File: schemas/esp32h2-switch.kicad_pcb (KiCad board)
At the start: 2 copper layers, 80.6 x 59.1 mm, 21 parts, among them J1 Screw_Terminal_01x02, J2 Screw_Terminal_01x02, J3 Conn_01x15, J4 Conn_01x15, K1 SPDT, 5V 72R, 10A 250VAC, Q1 NPN, 40V, 500mA, U1 LM1117MP-3.3

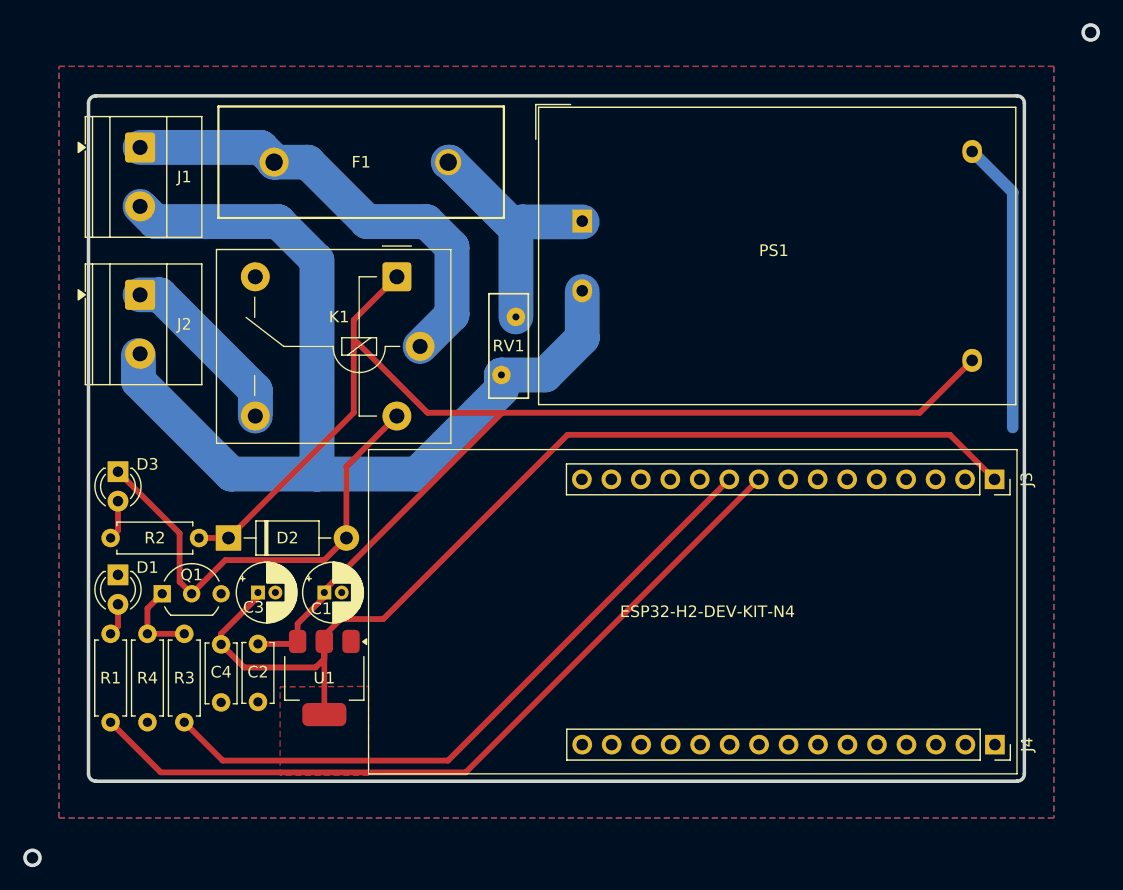
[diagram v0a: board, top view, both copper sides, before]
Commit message: Fix footprints and improve layout for hand soldering
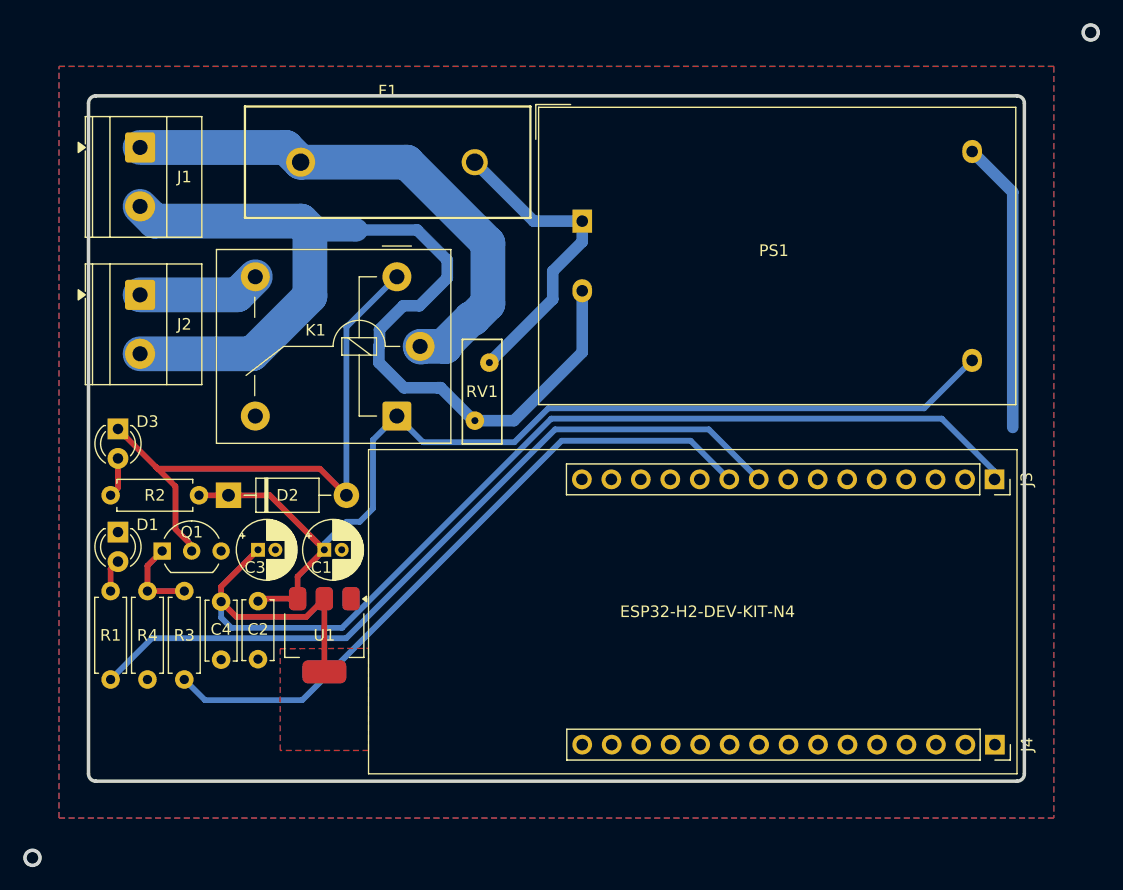
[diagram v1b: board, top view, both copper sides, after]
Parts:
- added NT1: NetTie_2, NetTie:NetTie-2_SMD_Pad2.0mm, B.Cu at (127.8, 85.9)
- C1, C3: footprint Sivakov_Capacitors_THT:CP_Radial_D5.0mm_P1.50mm -> KiCadX_Capacitors_THT:CP_Radial_D5.0mm_P1.50mm
- F1: footprint Sivakov_FuseHolders_THT:FuseHolder_THT_5x20mm_PTF76_RM15mm -> KiCadX_FuseHolders_THT:FuseHolder_THT_5x20mm_PTF76_RM15mm
- K1: footprint Sivakov_Relays_THT:Relay_SPDT_Relpol-RM51 -> KiCadX_Relays_THT:Relay_SPDT_Relpol-RM51
- moved RV1 4.55 mm to (141.2, 97.3)
- moved C2 3.68 mm to (121.3, 117.8)
- moved D3 3.68 mm to (109.2, 103.0)
- moved Q1 3.68 mm to (113.0, 113.5)
- moved R1 3.68 mm to (108.6, 117.0)
- moved R3 3.68 mm to (114.9, 124.6)
- moved R4 3.68 mm to (111.8, 117.0)
- moved C1 3.68 mm to (127.0, 113.4)
- moved C3 3.68 mm to (121.3, 113.4)
- moved C4 3.68 mm to (118.1, 117.9)
- moved D1 3.68 mm to (109.2, 111.9)
- moved D2 3.68 mm to (118.7, 108.7)
- moved R2 3.68 mm to (116.2, 108.7)
- moved U1 3.68 mm to (127.0, 120.8)
- moved F1 2.29 mm to (132.5, 80.0)
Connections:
- net /L renamed L
- J1 pad 2: N -> N_IN
- J2 pad 2: N -> N_IN
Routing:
- net N: track 89.0 -> 48.3 mm
- net N_IN: track 0.00 -> 37.9 mm
- net +5V: track 119.3 -> 89.6 mm
- net /RELAY_COIL: track 40.8 -> 51.2 mm
- net +3.3V: track 90.6 -> 100.6 mm
- net L_IN: track 40.2 -> 46.2 mm
- net L: track 21.8 -> 26.9 mm
- net /L_OUT: track 15.6 -> 10.6 mm
- net Net-(J3-Pin_9): track 68.1 -> 66.6 mm
